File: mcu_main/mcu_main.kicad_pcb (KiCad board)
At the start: 2 copper layers, 13.4 x 4.5 mm, 47 parts, among them J1 Micro_SD_Card_Det_Hirose_DM3AT, J2 Conn_01x10_Pin, J3 Conn_01x06_Pin, J4 4P4C_Shielded, J5 4P4C_Shielded, J6 Screw_Terminal_01x03_ebrake, J7 Screw_Terminal_01x03_throttle, J8 Screw_Terminal_01x06, J9 Conn_01x14_Socket, SW1 SW_Push_Dual, SW2 SW_Push_Dual, U1 ESP32-S3-WROOM-1, U2 USB_C_connector, U3 SGM2212-3.3, U4 VL53L1CXV0FY1

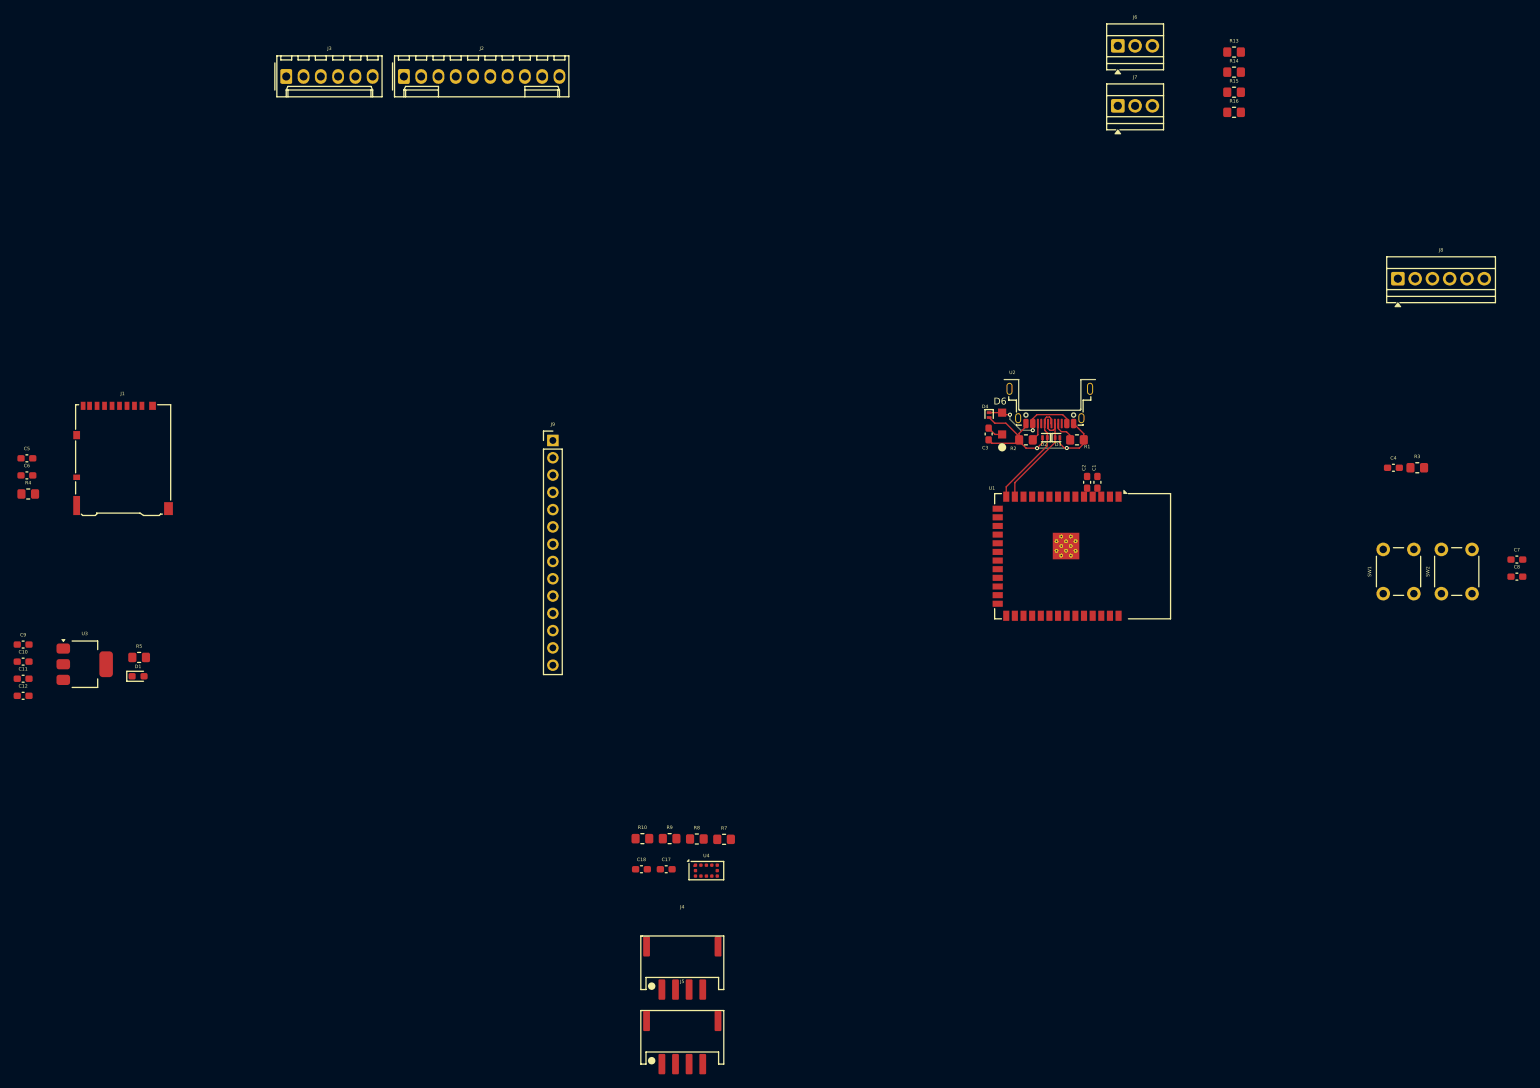
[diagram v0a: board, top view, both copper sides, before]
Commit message: fixed the power section of the pcb layout
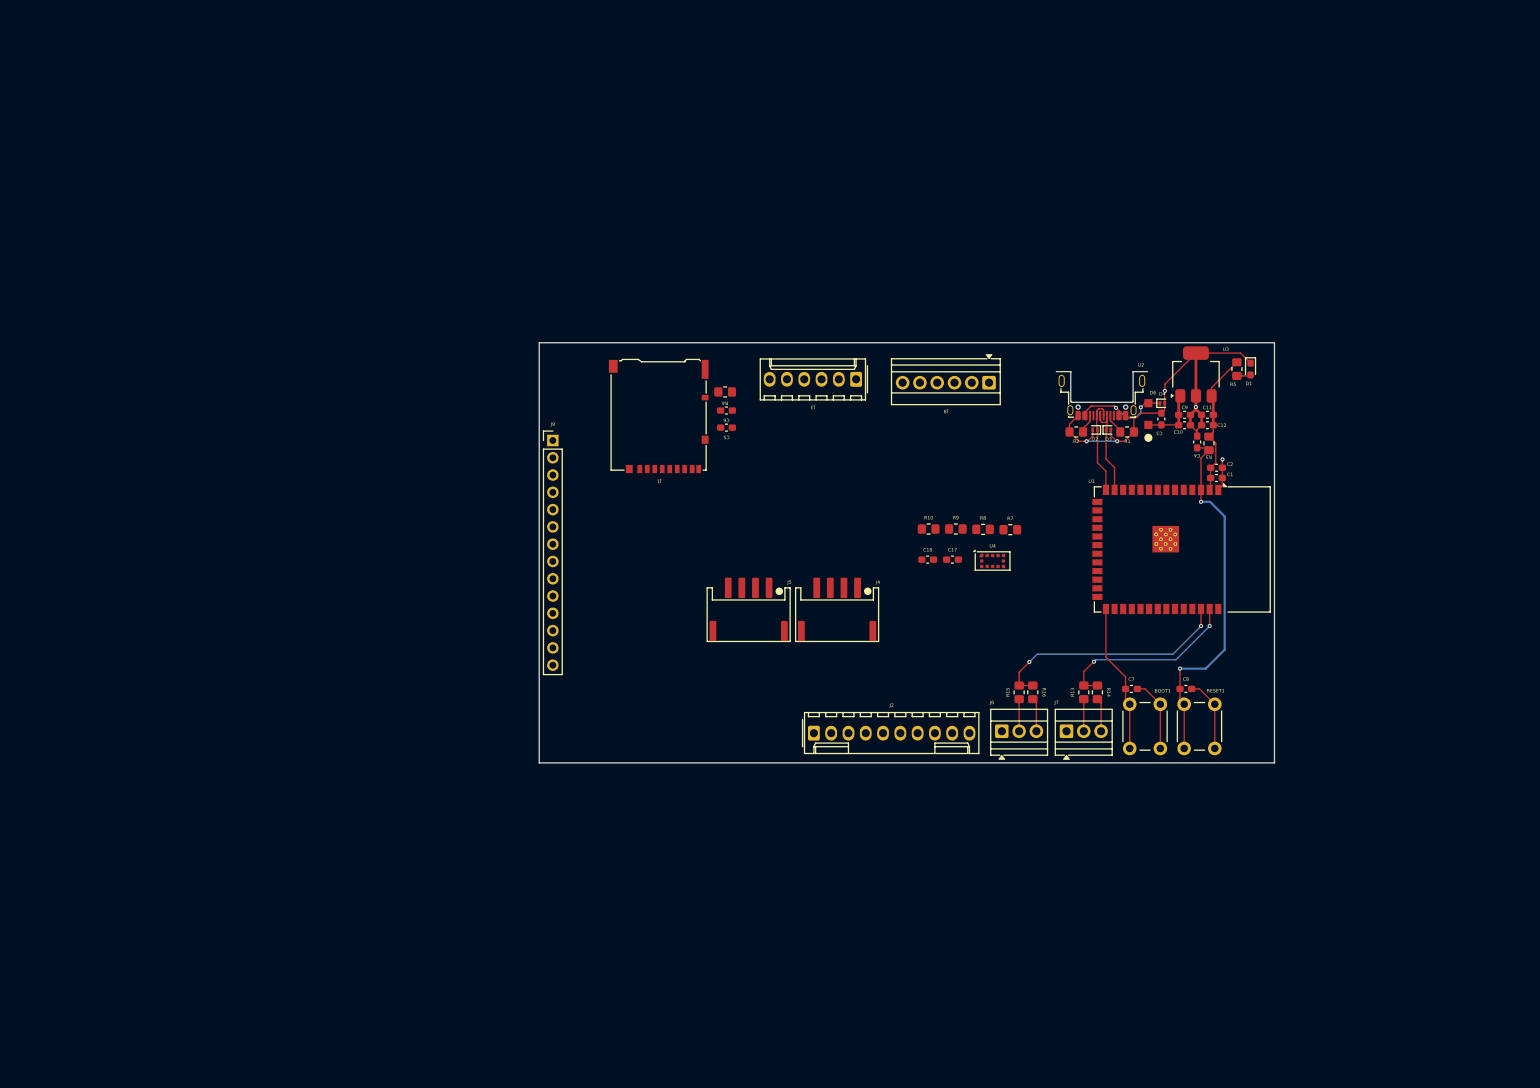
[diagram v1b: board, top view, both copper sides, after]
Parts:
- removed SW1, SW2: SW_Push_Dual, Button_Switch_THT:SW_PUSH_6mm
- added BOOT1: SW_Push_Dual, Button_Switch_THT:SW_PUSH_6mm, F.Cu at (186.8, 129.6)
- added RESET1: SW_Push_Dual, Button_Switch_THT:SW_PUSH_6mm, F.Cu at (194.8, 129.6)
- moved C12 178.5 mm to (198.2, 82.1)
- moved C11 178.3 mm to (198.2, 80.6)
- moved C10 174.2 mm to (194.8, 82.1)
- moved C9 174.0 mm to (194.8, 80.6)
- moved D1 169.6 mm to (204.5, 73.9), turned to -90 degrees
- moved U3 168.8 mm to (196.5, 74.7), turned to 90 degrees
- moved R5 166.8 mm to (202.5, 73.9), turned to -90 degrees
- moved J2 113.8 mm to (140.4, 127.4)
- moved R4 103.5 mm to (127.3, 77.2), turned to 180 degrees
- moved C6 103.2 mm to (127.5, 80.0), turned to 180 degrees
- moved C5 102.9 mm to (127.5, 82.5), turned to 180 degrees
- moved J6 102.1 mm to (168.0, 127.1)
- moved R13 96.6 mm to (180.0, 121.4), turned to 90 degrees
- moved J3 94.8 mm to (146.6, 75.4), turned to 180 degrees
- moved R15 93.7 mm to (170.5, 121.4), turned to 90 degrees
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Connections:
- J2 pad 10: RX_D0 -> TX_D0
- J2 pad 9: TX_D0 -> RX_D0
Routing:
- net GND: track 31.8 -> 101.0 mm, vias 2 -> 5
- net chip_pu: track 0.00 -> 54.2 mm, vias 0 -> 2
- net /Throttle and ebrake connectors/ebrake_sig: track 0.00 -> 36.0 mm, vias 0 -> 2
- net /Throttle and ebrake connectors/throttle_sig: track 0.00 -> 27.8 mm, vias 0 -> 2
- net GPIO_0: track 0.00 -> 21.9 mm
- net ESP_3v3: track 0.00 -> 21.4 mm
- net +5V: track 2.37 -> 8.88 mm
- net Net-(J7-Pin_2): track 0.00 -> 4.72 mm
- net Net-(J6-Pin_2): track 0.00 -> 4.72 mm
- net Net-(D1-A): track 0.00 -> 2.05 mm
- net /ESP USB section/D+: track 16.1 -> 14.2 mm
- net /ESP USB section/D-: track 15.9 -> 14.2 mm
- net Net-(U2-CC1): track 3.55 -> 3.01 mm
- net Net-(D6-A): track 15.8 -> 15.2 mm
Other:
- board size 13.4 x 4.5 mm -> 108 x 61.7 mm

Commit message: added most things to the pcb, review required
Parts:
- added J10: Conn_01x02_Pin, Connector_PinHeader_2.54mm:PinHeader_1x02_P2.54mm_Vertical, F.Cu at (129.0, 72.9)
- J2: footprint Connector_Molex:Molex_KK-254_AE-6410-10A_1x10_P2.54mm_Vertical -> Connector_PinHeader_2.54mm:PinHeader_1x10_P2.54mm_Vertical
- J3: footprint Connector_Molex:Molex_KK-254_AE-6410-06A_1x06_P2.54mm_Vertical -> Connector_PinHeader_2.54mm:PinHeader_1x06_P2.54mm_Vertical
- moved J2 32.1 mm to (108.2, 127.9), turned to 90 degrees
- moved R4 18.7 mm to (113.5, 89.9), turned to 0 degrees
- moved J4 18.1 mm to (152.7, 121.7)
- moved J5 18.1 mm to (139.7, 121.7)
- moved U4 14.9 mm to (152.0, 104.9), turned to 90 degrees
- moved R9 14.7 mm to (172.5, 106.8), turned to 90 degrees
- moved C6 14.5 mm to (118.5, 91.4), turned to 0 degrees
- moved R7 12.3 mm to (175.5, 108.1), turned to 90 degrees
- moved C5 11.6 mm to (118.5, 89.8), turned to 0 degrees
- moved R10 11.5 mm to (166.5, 104.3), turned to 90 degrees
- moved C17 11.0 mm to (152.8, 109.5), turned to 90 degrees
- moved C18 9.60 mm to (151.3, 109.5), turned to 90 degrees
- moved R8 9.19 mm to (169.5, 105.6), turned to 90 degrees
- moved R15 5.27 mm to (165.3, 121.1)
- moved R16 5.27 mm to (167.3, 121.1)
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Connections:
- J1 pad 2: FSPIQ_MISO -> sdcard_CS
- J1 pad 7: FSPICS0 -> FSPIQ_MISO
- J3 pad 1: GPIO_15 -> GPIO_7
- J3 pad 2: GPIO_16 -> GPIO_15
- J3 pad 3: GPIO_17 -> GPIO_16
- J3 pad 4: GPIO_18 -> GPIO_17
- J3 pad 5: GPIO_3 -> GPIO_18
- J3 pad 6: GPIO_21 -> GPIO_8
- J8 pad 3: /PAS connector/speed_sig_2 -> /PAS connector/speed_sig_1
- J8 pad 4: /PAS connector/speed_sig_1 -> /PAS connector/speed_sig_2
- J9 pad 3: Display_CS -> FSPICS0
- R10 pad 2: /Time of flight sensor/TOF_XSHUT -> TOF_XSHUT
- R4 pad 2: FSPIQ_MISO -> sdcard_CS
- U1 pad 12: Display_DC/RS -> GPIO_8
- U1 pad 15: GPIO_3 -> sdcard_CS
- U1 pad 16: /Time of flight sensor/TOF_GPIO1 -> Display_RST
- U1 pad 17: Display_LED -> Display_DC/RS
- U1 pad 22: Display_CS -> Display_LED
- U1 pad 23: GPIO_21 -> TOF_XSHUT
- U1 pad 26: /Time of flight sensor/TOF_XSHUT -> /Time of flight sensor/TOF_GPIO1
- U1 pad 7: Display_RST -> GPIO_7
- U4 pad 5: /Time of flight sensor/TOF_XSHUT -> TOF_XSHUT
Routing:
- net +5V: track 8.88 -> 239.5 mm
- net FSPIQ_MISO: track 0.00 -> 91.4 mm, vias 0 -> 2
- net FSPICLK: track 0.00 -> 89.8 mm, vias 0 -> 3
- net FSPID_MOSI: track 0.00 -> 87.0 mm, vias 0 -> 3
- net GPIO_35: track 0.00 -> 80.8 mm, vias 0 -> 1
- net GPIO_36: track 0.00 -> 79.5 mm, vias 0 -> 1
- net FSPICS0: track 0.00 -> 78.9 mm, vias 0 -> 1
- net GPIO_37: track 0.00 -> 78.2 mm, vias 0 -> 1
- net GPIO_38: track 0.00 -> 77.0 mm, vias 0 -> 1
- net Display_RST: track 0.00 -> 76.8 mm, vias 0 -> 1
- net Display_DC/RS: track 0.00 -> 76.2 mm, vias 0 -> 1
- net Display_LED: track 0.00 -> 76.0 mm, vias 0 -> 1
- net GPIO_39: track 0.00 -> 75.7 mm, vias 0 -> 1
- net GPIO_40: track 0.00 -> 74.4 mm, vias 0 -> 1
- net GPIO_41: track 0.00 -> 73.2 mm, vias 0 -> 1
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- added copper zone on F.Cu, net ESP_3v3
- added copper zone on B.Cu, net GND
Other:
- outline, holes or cut-outs redrawn
- board text added: "Ebrake"
- board text added: "FSPI_CLK"
- board text added: "FSPI_MISO"
- board text added: "FSPI_MOSI"
- board text added: "I2C_SCL"
- board text added: "I2C_SDA"
- board text added: "Throttle"

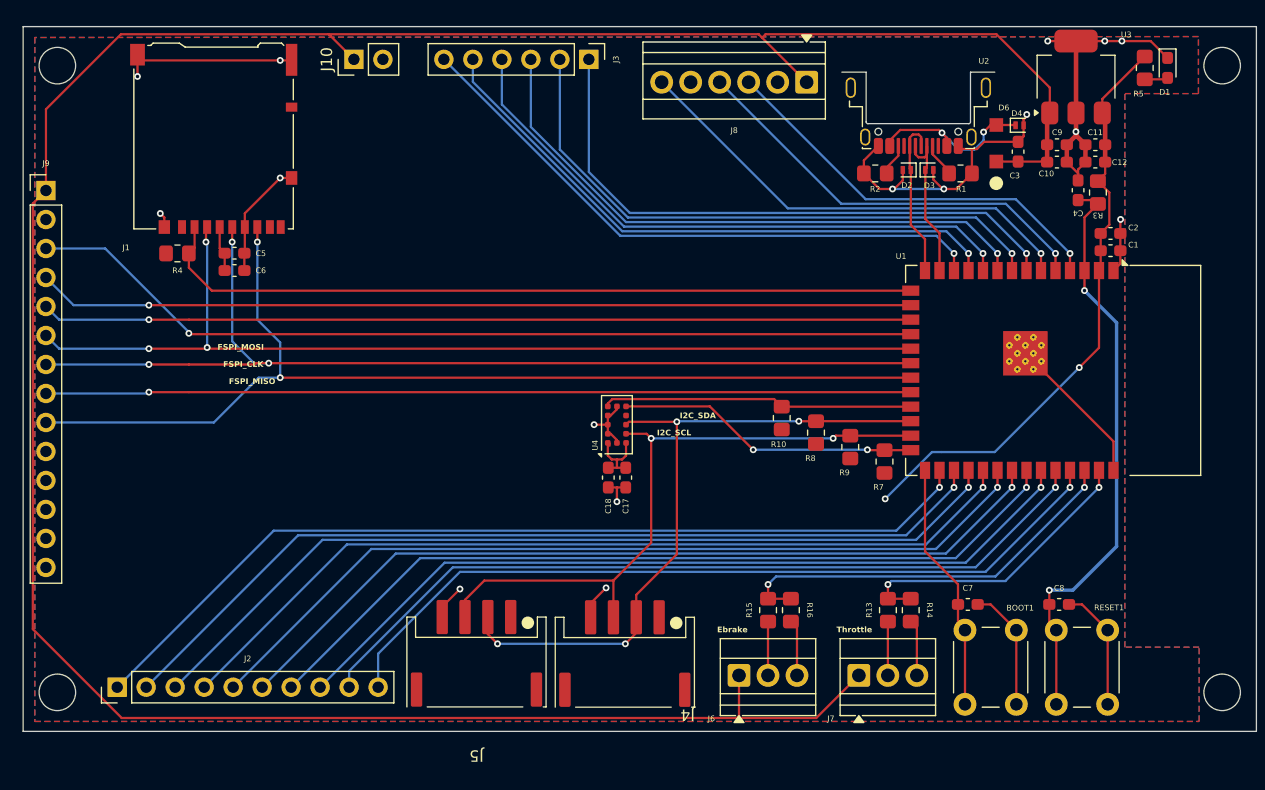
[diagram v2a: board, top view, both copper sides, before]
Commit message: Fixed most drc violations
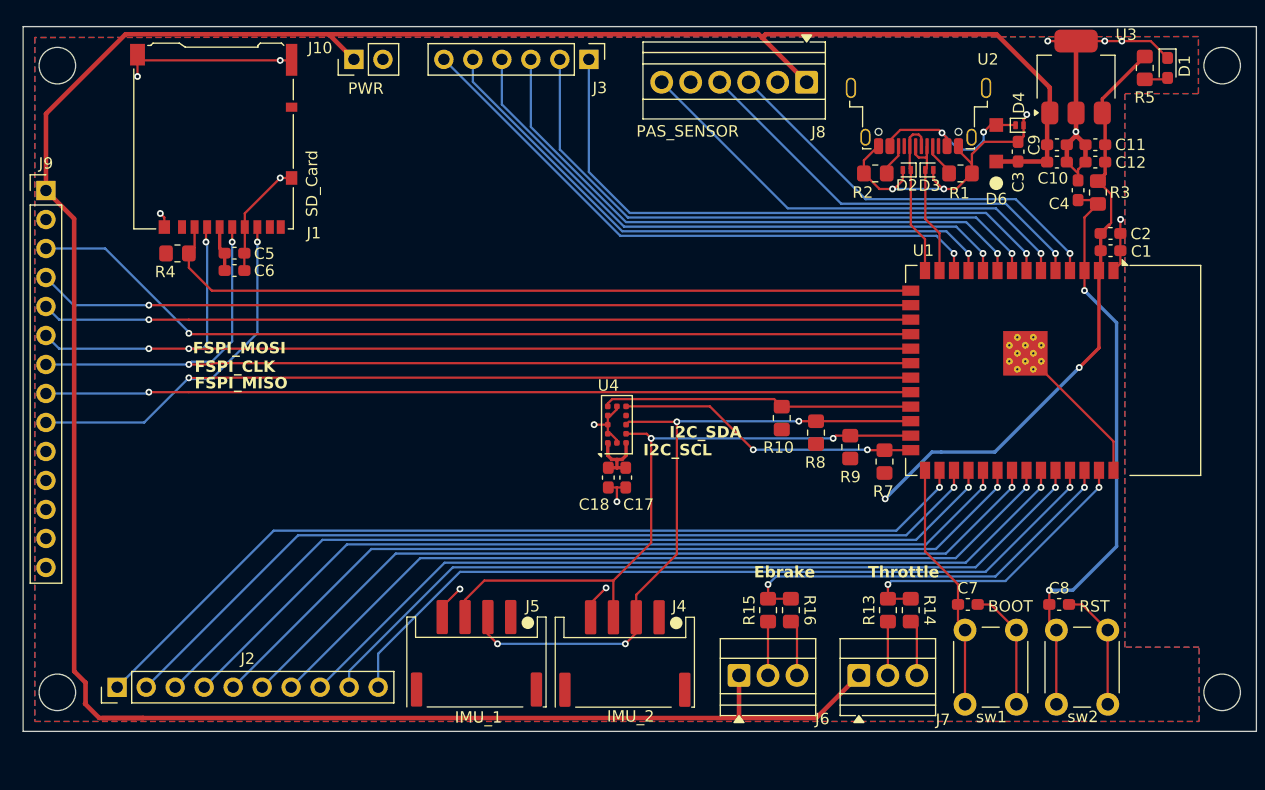
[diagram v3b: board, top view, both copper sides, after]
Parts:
- removed BOOT1, RESET1: SW_Push_Dual, Button_Switch_THT:SW_PUSH_6mm
- added sw1: SW_Push_Dual, Button_Switch_THT:SW_PUSH_6mm, F.Cu at (182.5, 129.4)
- added sw2: SW_Push_Dual, Button_Switch_THT:SW_PUSH_6mm, F.Cu at (190.5, 129.4)
- U2: footprint Connector_USB:USB_C_Receptacle_Amphenol_12401948E412A -> Custom_footprints:USB_C_Receptacle_Amphenol_12401948E412A_editted
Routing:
- net +5V: track 239.5 -> 243.1 mm
- net FSPIQ_MISO: track 91.4 -> 94.4 mm
- net GND: track 150.5 -> 152.2 mm
- net FSPID_MOSI: track 87.0 -> 88.3 mm
- net /ESP USB section/D-: track 14.2 -> 14.8 mm
- net FSPICLK: track 89.8 -> 90.5 mm, vias 3 -> 2
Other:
- board text added: "BOOT"
- board text added: "IMU_1"
- board text added: "IMU_2"
- board text added: "PAS_SENSOR"
- board text added: "PWR"
- board text added: "RST"
- board text added: "SD_Card"
